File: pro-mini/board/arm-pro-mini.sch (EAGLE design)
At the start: 55 parts, among them J1 USB, J2 SWD HEADER, Q1 12Mhz, T1 DTA114EET1G (2 X 10K), U1 MCP1754ST-3302E/CB, U2 NUF2042XV6T1G, U3 LPC11U35FHI33/501

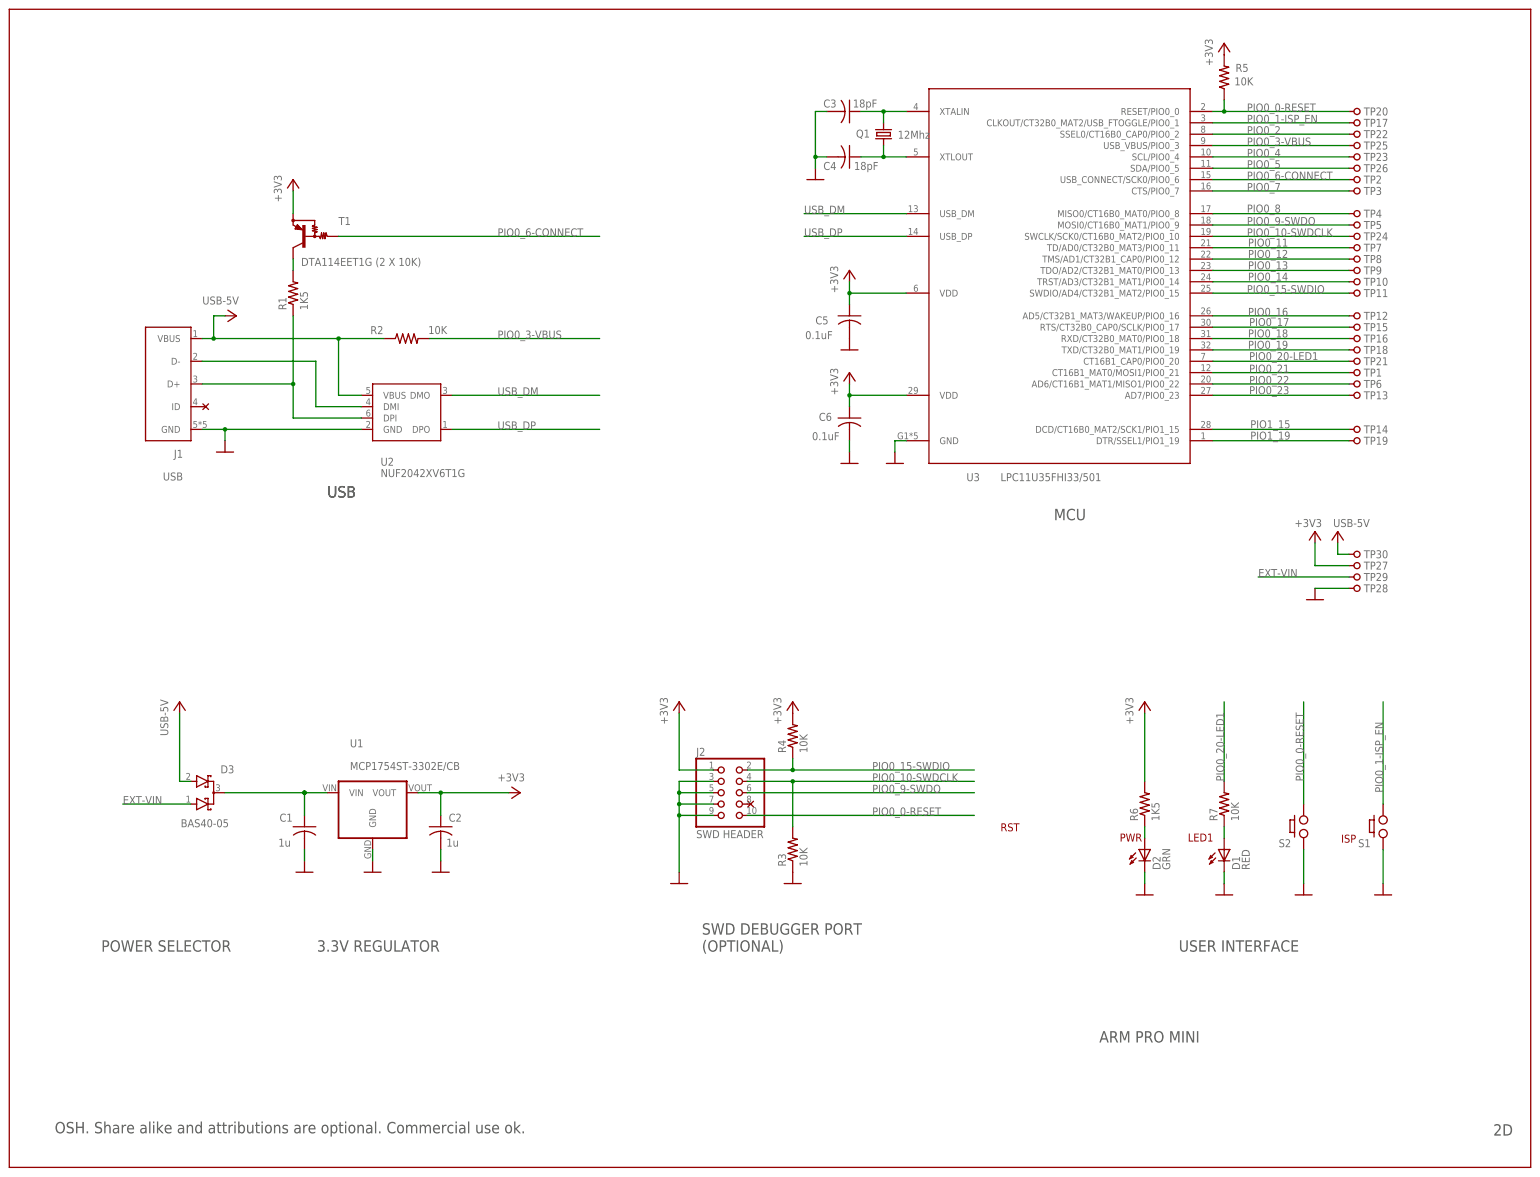
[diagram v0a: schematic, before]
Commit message: Updated revision Renamed directory from eagle to board. Added tester board.
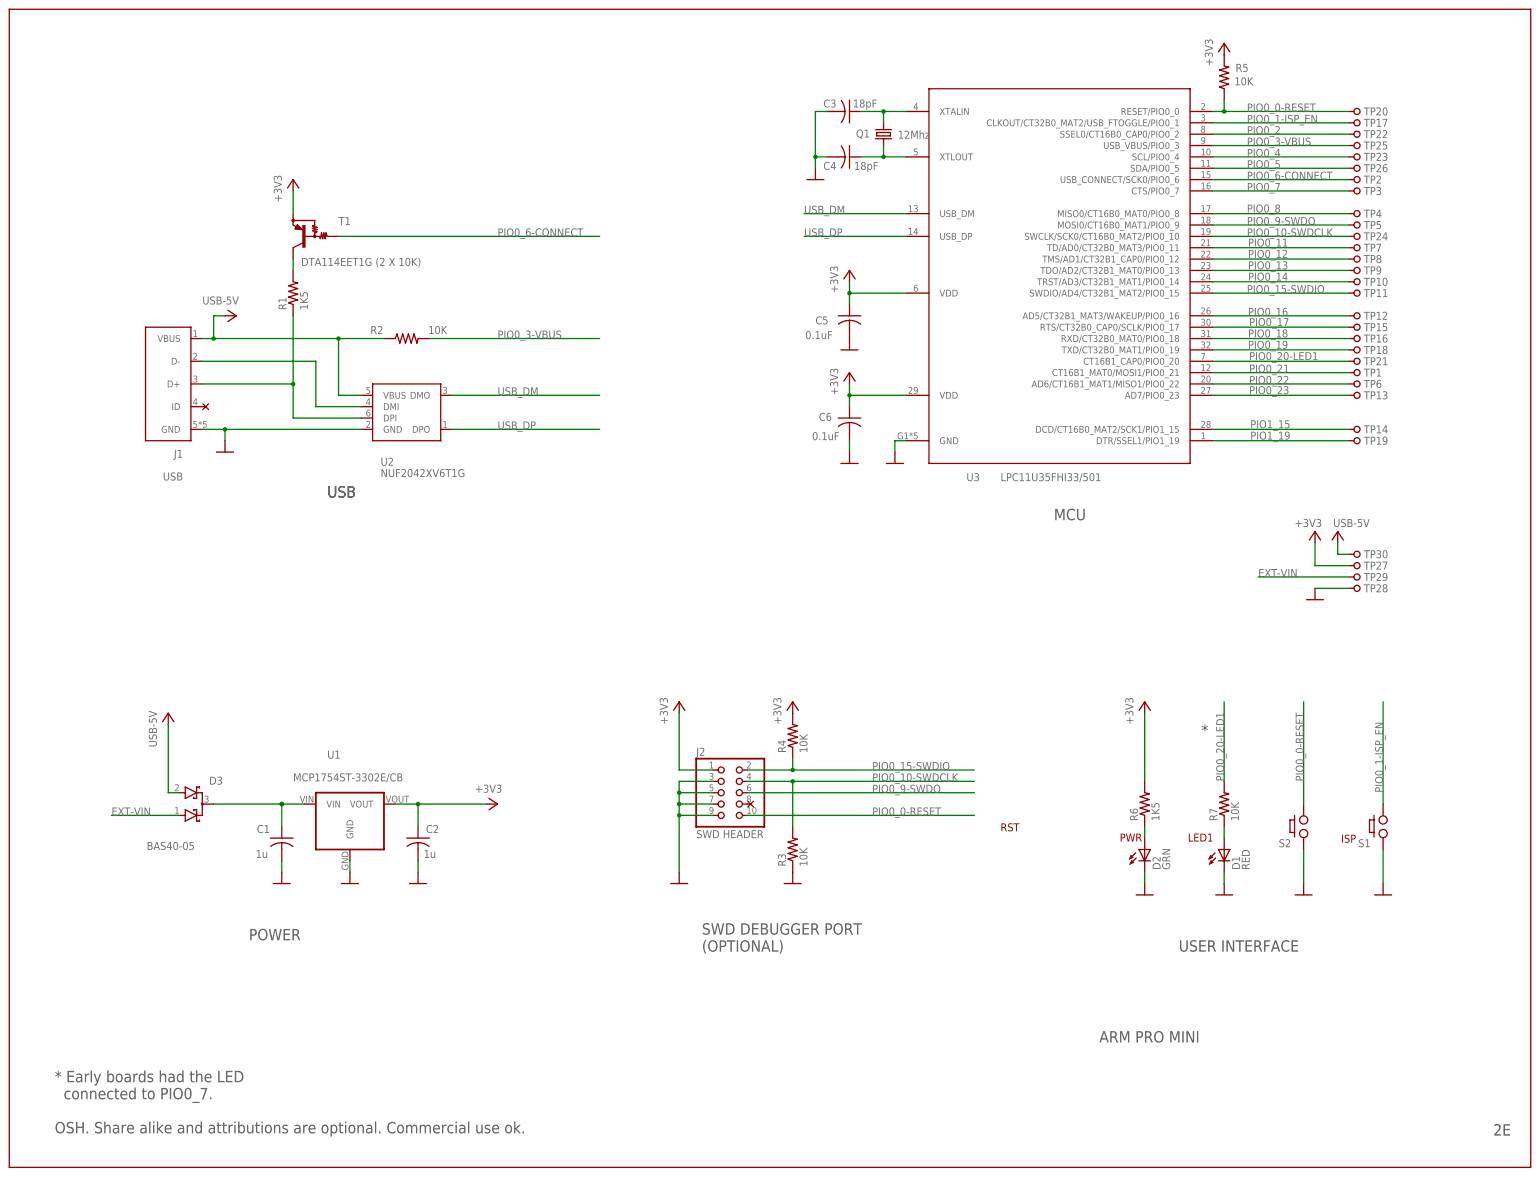
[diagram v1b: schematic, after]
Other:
- note added: "*"
- note added: "* Early boards had the LED connected to PIO0_7."
- note added: "2E"
- note added: "POWER"
- note removed: "2D"
- note removed: "3.3V REGULATOR"
- note removed: "POWER SELECTOR"
- moved on the sheet: C1, C2, D3, U1
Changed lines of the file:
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@@
 <wire x1="0" y1="0" x2="0" y2="259.08" width="0.1524" layer="94"/>
 <text x="233.68" y="144.78" size="2.54" layer="97">MCU</text>
-<text x="331.978" y="7.112" size="2.54" layer="97">2D</text>
-<text x="68.834" y="48.26" size="2.54" layer="97">3.3V REGULATOR</text>
+<text x="331.978" y="7.112" size="2.54" layer="97">2E</text>
 <text x="71.12" y="149.86" size="2.54" layer="97">USB</text>
 <text x="154.94" y="48.26" size="2.54" layer="97">SWD DEBUGGER PORT
@@
 <text x="248.412" y="72.898" size="1.778" layer="94">PWR</text>
 <text x="261.62" y="48.26" size="2.54" layer="97">USER INTERFACE</text>
-<text x="20.574" y="48.26" size="2.54" layer="97">POWER SELECTOR</text>
+<text x="53.594" y="50.8" size="2.54" layer="97">POWER</text>
 <text x="10.16" y="7.62" size="2.54" layer="97" font="vector">OSH. Share alike and attributions are optional. Commercial use ok.</text>
 <text x="71.12" y="149.86" size="2.54" layer="97">USB</text>
+<text x="10.16" y="15.24" size="2.54" layer="97">* Early boards had the LED
+  connected to PIO0_7.</text>
+<text x="266.7" y="96.52" size="2.54" layer="97">*</text>
 </plain>
 <instances>
@@
 <attribute name="NAME" x="301.752" y="71.628" size="1.778" layer="95"/>
 </instance>
-<instance part="GND3" gate="1" x="81.28" y="66.04"/>
-<instance part="C2" gate="G$1" x="96.52" y="76.2" smashed="yes">
-<attribute name="NAME" x="98.298" y="77.343" size="1.778" layer="95"/>
-<attribute name="VALUE" x="97.79" y="71.755" size="1.778" layer="96"/>
-</instance>
-<instance part="GND18" gate="1" x="96.52" y="66.04"/>
-<instance part="C1" gate="G$1" x="66.04" y="76.2" smashed="yes">
-<attribute name="NAME" x="60.452" y="77.343" size="1.778" layer="95"/>
-<attribute name="VALUE" x="60.198" y="71.755" size="1.778" layer="96"/>
-</instance>
-<instance part="GND28" gate="1" x="66.04" y="66.04"/>
+<instance part="GND3" gate="1" x="76.2" y="63.5"/>
+<instance part="C2" gate="G$1" x="91.44" y="73.66" smashed="yes">
+<attribute name="NAME" x="93.218" y="74.803" size="1.778" layer="95"/>
+<attribute name="VALUE" x="92.71" y="69.215" size="1.778" layer="96"/>
+</instance>
+<instance part="GND18" gate="1" x="91.44" y="63.5"/>
+<instance part="C1" gate="G$1" x="60.96" y="73.66" smashed="yes">
+<attribute name="NAME" x="55.372" y="74.803" size="1.778" layer="95"/>
+<attribute name="VALUE" x="55.118" y="69.215" size="1.778" layer="96"/>
+</instance>
+<instance part="GND28" gate="1" x="60.96" y="63.5"/>
 <instance part="U3" gate="G$1" x="254" y="190.5" smashed="yes">
 <attribute name="NAME" x="214.122" y="153.5176" size="1.778" layer="95"/>
@@
 <attribute name="VALUE" x="43.18" y="193.04" size="1.778" layer="96"/>
 </instance>
-<instance part="+3V5" gate="G$1" x="114.3" y="83.82" rot="R270"/>
+<instance part="+3V5" gate="G$1" x="109.22" y="81.28" rot="R270"/>
 <instance part="J2" gate="A" x="160.02" y="83.82"/>
 <instance part="+3V6" gate="G$1" x="149.86" y="104.14"/>
@@
 <instance part="GND6" gate="1" x="271.78" y="60.96"/>
 <instance part="+3V4" gate="G$1" x="254" y="104.14"/>
-<instance part="D3" gate="G$1" x="43.18" y="83.82" smashed="yes" rot="MR180">
-<attribute name="NAME" x="47.244" y="89.9414" size="1.778" layer="95" rot="MR180"/>
-<attribute name="VALUE" x="38.354" y="77.8764" size="1.778" layer="96" rot="MR180"/>
-</instance>
-<instance part="P+1" gate="VCC" x="38.1" y="104.14" smashed="yes">
-<attribute name="VALUE" x="35.56" y="96.52" size="1.778" layer="96" rot="R90"/>
+<instance part="D3" gate="G$1" x="40.64" y="81.28" smashed="yes" rot="MR180">
+<attribute name="NAME" x="44.704" y="87.4014" size="1.778" layer="95" rot="MR180"/>
+<attribute name="VALUE" x="30.734" y="72.7964" size="1.778" layer="96" rot="MR180"/>
+</instance>
+<instance part="P+1" gate="VCC" x="35.56" y="101.6" smashed="yes">
+<attribute name="VALUE" x="33.02" y="93.98" size="1.778" layer="96" rot="R90"/>
 </instance>
 <instance part="TP20" gate="G$1" x="302.26" y="236.22"/>
@@
 <instance part="D1" gate="G$1" x="271.78" y="71.12"/>
 <instance part="D2" gate="G$1" x="254" y="71.12"/>
-<instance part="U1" gate="G$1" x="81.28" y="78.74" smashed="yes">
-<attribute name="NAME" x="76.2" y="93.98" size="1.778" layer="95"/>
-<attribute name="VALUE" x="76.2" y="88.9" size="1.778" layer="96"/>
+<instance part="U1" gate="G$1" x="76.2" y="76.2" smashed="yes">
+<attribute name="NAME" x="71.12" y="91.44" size="1.778" layer="95"/>
+<attribute name="VALUE" x="63.5" y="86.36" size="1.778" layer="96"/>
 </instance>
 <instance part="J1" gate="G$1" x="35.56" y="170.18"/>
@@
 </segment>
 <segment>
-<wire x1="81.28" y1="71.12" x2="81.28" y2="68.58" width="0.1524" layer="91"/>
+<wire x1="76.2" y1="68.58" x2="76.2" y2="66.04" width="0.1524" layer="91"/>
 <pinref part="GND3" gate="1" pin="GND"/>
 <pinref part="U1" gate="G$1" pin="GND"/>
@@
 <pinref part="C2" gate="G$1" pin="2"/>
 <pinref part="GND18" gate="1" pin="GND"/>
-<wire x1="96.52" y1="71.12" x2="96.52" y2="68.58" width="0.1524" layer="91"/>
+<wire x1="91.44" y1="68.58" x2="91.44" y2="66.04" width="0.1524" layer="91"/>
 </segment>
 <segment>
 <pinref part="GND28" gate="1" pin="GND"/>
 <pinref part="C1" gate="G$1" pin="2"/>
-<wire x1="66.04" y1="68.58" x2="66.04" y2="71.12" width="0.1524" layer="91"/>
+<wire x1="60.96" y1="66.04" x2="60.96" y2="68.58" width="0.1524" layer="91"/>
 </segment>
 <segment>
@@
 </segment>
 <segment>
-<wire x1="91.44" y1="83.82" x2="96.52" y2="83.82" width="0.1524" layer="91"/>
+<wire x1="86.36" y1="81.28" x2="91.44" y2="81.28" width="0.1524" layer="91"/>
 <pinref part="C2" gate="G$1" pin="1"/>
-<wire x1="96.52" y1="83.82" x2="111.76" y2="83.82" width="0.1524" layer="91"/>
-<wire x1="96.52" y1="78.74" x2="96.52" y2="83.82" width="0.1524" layer="91"/>
-<junction x="96.52" y="83.82"/>
+<wire x1="91.44" y1="81.28" x2="106.68" y2="81.28" width="0.1524" layer="91"/>
+<wire x1="91.44" y1="76.2" x2="91.44" y2="81.28" width="0.1524" layer="91"/>
+<junction x="91.44" y="81.28"/>
 <pinref part="+3V5" gate="G$1" pin="+3V3"/>
 <pinref part="U1" gate="G$1" pin="VOUT"/>
@@
 <segment>
 <pinref part="D3" gate="G$1" pin="A2"/>
-<wire x1="40.64" y1="86.36" x2="38.1" y2="86.36" width="0.1524" layer="91"/>
-<wire x1="38.1" y1="86.36" x2="38.1" y2="101.6" width="0.1524" layer="91"/>
+<wire x1="38.1" y1="83.82" x2="35.56" y2="83.82" width="0.1524" layer="91"/>
+<wire x1="35.56" y1="83.82" x2="35.56" y2="99.06" width="0.1524" layer="91"/>
 <pinref part="P+1" gate="VCC" pin="USB-5V"/>
 </segment>
@@
 <net name="N$10" class="0">
 <segment>
-<wire x1="71.12" y1="83.82" x2="66.04" y2="83.82" width="0.1524" layer="91"/>
+<wire x1="66.04" y1="81.28" x2="60.96" y2="81.28" width="0.1524" layer="91"/>
 <pinref part="C1" gate="G$1" pin="1"/>
-<wire x1="66.04" y1="78.74" x2="66.04" y2="83.82" width="0.1524" layer="91"/>
+<wire x1="60.96" y1="76.2" x2="60.96" y2="81.28" width="0.1524" layer="91"/>
 <pinref part="D3" gate="G$1" pin="C"/>
-<junction x="66.04" y="83.82"/>
-<junction x="66.04" y="83.82"/>
-<wire x1="48.26" y1="83.82" x2="66.04" y2="83.82" width="0.1524" layer="91"/>
+<junction x="60.96" y="81.28"/>
+<junction x="60.96" y="81.28"/>
+<wire x1="45.72" y1="81.28" x2="60.96" y2="81.28" width="0.1524" layer="91"/>
 <pinref part="U1" gate="G$1" pin="VIN"/>
 </segment>
@@
 <segment>
 <pinref part="D3" gate="G$1" pin="A1"/>
-<wire x1="40.64" y1="81.28" x2="25.4" y2="81.28" width="0.1524" layer="91"/>
-<label x="25.4" y="81.28" size="1.778" layer="95"/>
-</segment>
-</net>
+<wire x1="38.1" y1="78.74" x2="22.86" y2="78.74" width="0.1524" layer="91"/>
+<label x="22.86" y="78.74" size="1.778" layer="95"/>
+</segment>
+</net>

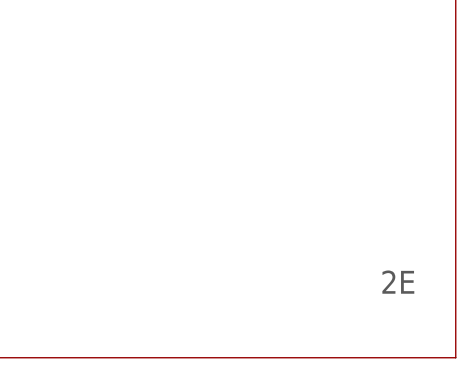
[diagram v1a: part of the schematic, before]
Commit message: Cleaned up top silkscreen from pads. Bumbed version from 2E to 2F. No stencil change. No semantic change.
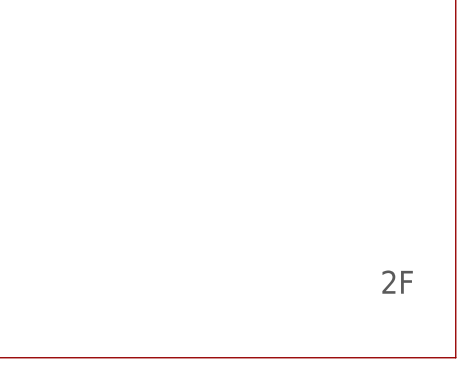
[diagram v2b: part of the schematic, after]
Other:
- note added: "2F"
- note removed: "2E"
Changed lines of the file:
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@@
 <wire x1="0" y1="0" x2="0" y2="259.08" width="0.1524" layer="94"/>
 <text x="233.68" y="144.78" size="2.54" layer="97">MCU</text>
-<text x="331.978" y="7.112" size="2.54" layer="97">2E</text>
+<text x="331.978" y="7.112" size="2.54" layer="97">2F</text>
 <text x="71.12" y="149.86" size="2.54" layer="97">USB</text>
 <text x="154.94" y="48.26" size="2.54" layer="97">SWD DEBUGGER PORT
